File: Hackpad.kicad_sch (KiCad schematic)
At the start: 10 parts, among them SW1 SW_Push, SW2 SW_Push, SW3 SW_Push, SW4 SW_Push, SW5 SW_Push, SW6 RotaryEncoder_Switch_MP, U1 XIAO-RP2040-DIP

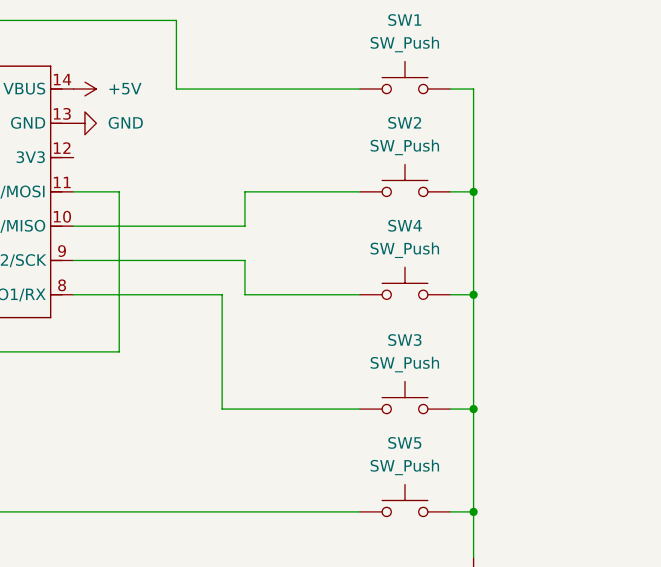
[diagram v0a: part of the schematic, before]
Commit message: Rotate oled & reroute
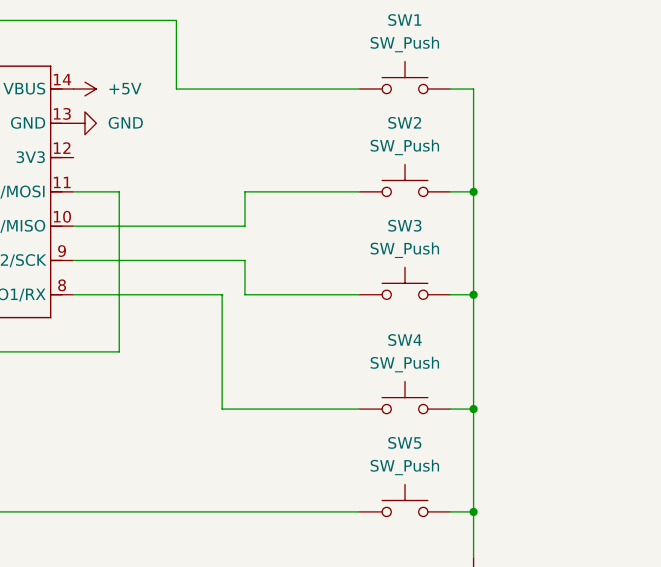
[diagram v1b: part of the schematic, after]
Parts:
- renumbered SW4 to SW3, SW3 to SW4
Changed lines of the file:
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@@
 		(dnp no)
 		(fields_autoplaced yes)
-		(property "Reference" "SW3"
+		(property "Reference" "SW4"
 			(at 220.98 100.33 0)
 			(effects
@@
 			(project "Hackpad"
 				(path "/a2f23f61-3e8c-4dfe-96db-54432bd0028a"
-					(reference "SW3")
+					(reference "SW4")
 					(unit 1)
 				)
@@
 		(dnp no)
 		(fields_autoplaced yes)
-		(property "Reference" "SW4"
+		(property "Reference" "SW3"
 			(at 220.98 87.63 0)
 			(effects
@@
 			(project "Hackpad"
 				(path "/a2f23f61-3e8c-4dfe-96db-54432bd0028a"
-					(reference "SW4")
-					(unit 1)
-				)
+					(reference "SW3")
+					(unit 1)
+				)

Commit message: 3D models & replace MX switch footprint
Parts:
- SW1, SW2, SW3, SW4, SW5: footprint Button_Switch_Keyboard:SW_Cherry_MX_1.00u_PCB -> Cherry MX:SW_Cherry_MX_PCB_1.00u
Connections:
- net GND: now also SW1.2, SW2.2, SW3.2, SW4.2, SW5.2; no longer SW1.1, SW2.1, SW3.1, SW4.1, SW5.1
- net at U1.10 (GPIO4/MISO): now also SW2.1; no longer SW2.2
- net at U1.8 (GPIO1/RX): now also SW4.1; no longer SW4.2
- net at U1.7 (GPIO0/TX): now also SW5.1; no longer SW5.2
- net at U1.9 (GPIO2/SCK): now also SW3.1; no longer SW3.2
- net at U1.4 (GPIO29/ADC3/A3): now also SW1.1; no longer SW1.2
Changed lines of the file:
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@@
 		(lib_id "Switch:SW_Push")
 		(at 220.98 83.82 0)
-		(mirror y)
 		(unit 1)
 		(exclude_from_sim no)
@@
 			)
 		)
-		(property "Footprint" "Button_Switch_Keyboard:SW_Cherry_MX_1.00u_PCB"
+		(property "Footprint" "Cherry MX:SW_Cherry_MX_PCB_1.00u"
 			(at 220.98 78.74 0)
 			(effects
@@
 		(lib_id "Switch:SW_Push")
 		(at 220.98 107.95 0)
-		(mirror y)
 		(unit 1)
 		(exclude_from_sim no)
@@
 			)
 		)
-		(property "Footprint" "Button_Switch_Keyboard:SW_Cherry_MX_1.00u_PCB"
+		(property "Footprint" "Cherry MX:SW_Cherry_MX_PCB_1.00u"
 			(at 220.98 102.87 0)
 			(effects
@@
 		(lib_id "Switch:SW_Push")
 		(at 220.98 119.38 0)
-		(mirror y)
 		(unit 1)
 		(exclude_from_sim no)
@@
 			)
 		)
-		(property "Footprint" "Button_Switch_Keyboard:SW_Cherry_MX_1.00u_PCB"
+		(property "Footprint" "Cherry MX:SW_Cherry_MX_PCB_1.00u"
 			(at 220.98 114.3 0)
 			(effects
@@
 		(lib_id "Switch:SW_Push")
 		(at 220.98 95.25 0)
-		(mirror y)
 		(unit 1)
 		(exclude_from_sim no)
@@
 			)
 		)
-		(property "Footprint" "Button_Switch_Keyboard:SW_Cherry_MX_1.00u_PCB"
+		(property "Footprint" "Cherry MX:SW_Cherry_MX_PCB_1.00u"
 			(at 220.98 90.17 0)
 			(effects
@@
 		(lib_id "Switch:SW_Push")
 		(at 220.98 72.39 0)
-		(mirror y)
 		(unit 1)
 		(exclude_from_sim no)
@@
 			)
 		)
-		(property "Footprint" "Button_Switch_Keyboard:SW_Cherry_MX_1.00u_PCB"
+		(property "Footprint" "Cherry MX:SW_Cherry_MX_PCB_1.00u"
 			(at 220.98 67.31 0)
 			(effects
